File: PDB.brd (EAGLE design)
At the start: 130.3 x 166.9 mm, 49 parts, among them J1 B06B-HCMKK, J2 B06B-HCMKK, J3 SS-6488-NF-A431, J4 SS-6488-NF-A431, J5 B06B-HCMKK, J6 B03B-HCMKS, J7 B03B-HCMKS, J8 SS-6488-NF-A431

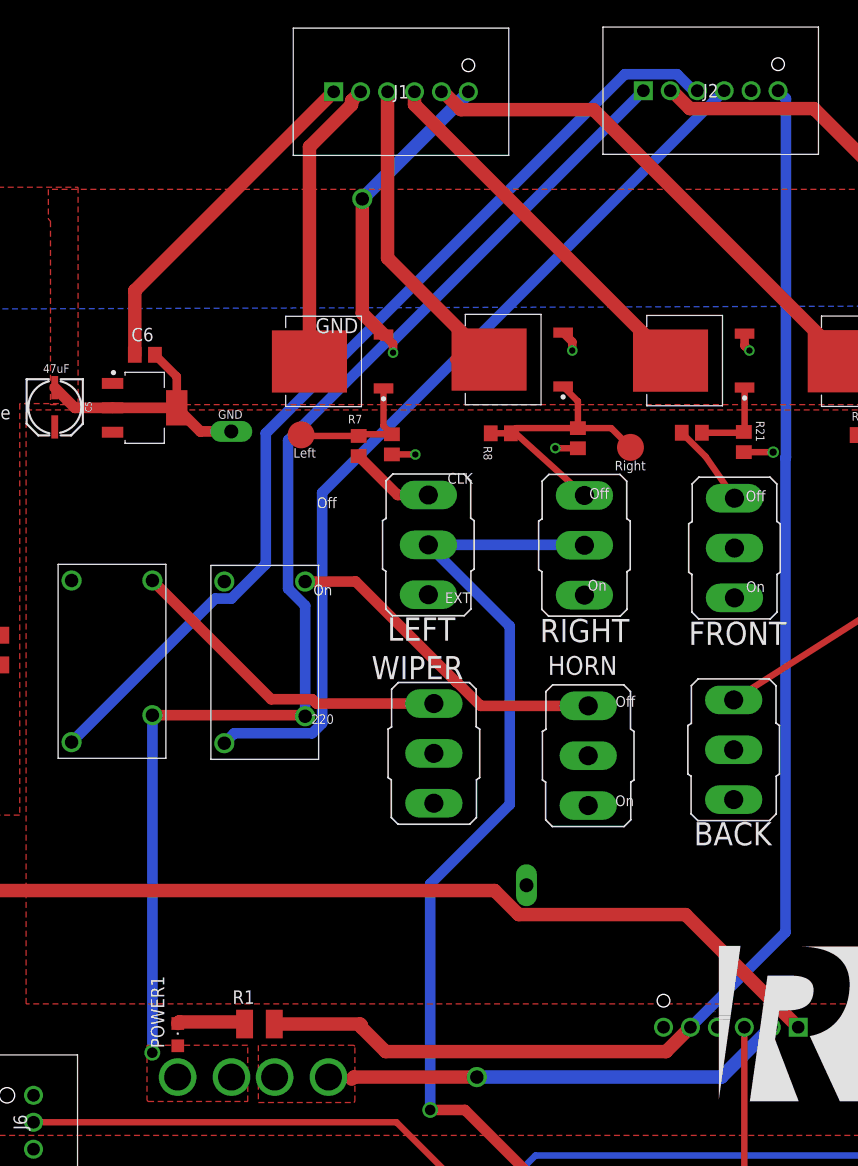
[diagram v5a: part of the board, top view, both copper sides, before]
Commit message: Widen the traces of independent 12V and indipendent ground
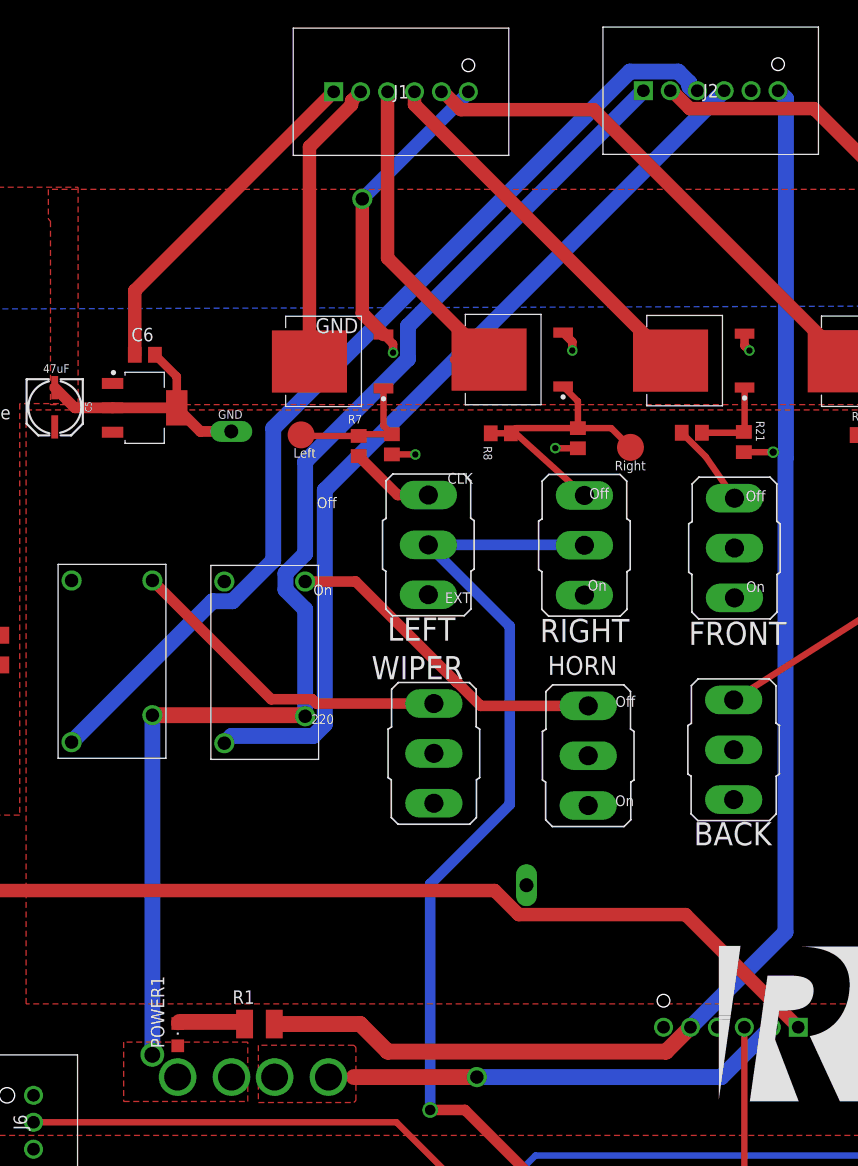
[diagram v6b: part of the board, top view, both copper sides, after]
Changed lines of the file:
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@@
 <vertex x="41.2" y="47.3"/>
 <vertex x="50.2" y="47.3"/>
-<vertex x="50.3" y="47.4"/>
-<vertex x="50.3" y="52.6"/>
+<vertex x="50.4" y="47.5"/>
+<vertex x="50.4" y="52.5"/>
 <vertex x="50.2" y="52.7"/>
 </polygon>
-<wire x1="89.56" y1="54.4" x2="84.86" y2="49.7" width="1.27" layer="16"/>
-<wire x1="84.86" y1="49.7" x2="61.8" y2="49.7" width="1.27" layer="16"/>
+<wire x1="89.56" y1="54.4" x2="84.86" y2="49.7" width="1.5" layer="16"/>
+<wire x1="84.86" y1="49.7" x2="61.8" y2="49.7" width="1.5" layer="16"/>
 <via x="61.8" y="49.7" extent="1-16" drill="1.27"/>
-<wire x1="61.8" y1="49.7" x2="50.2" y2="49.7" width="1.27" layer="1"/>
-<wire x1="50.2" y1="49.7" x2="50" y2="49.5" width="1.27" layer="1"/>
+<wire x1="61.8" y1="49.7" x2="50.2" y2="49.7" width="1.5" layer="1"/>
+<wire x1="47.812" y1="49.7" x2="50.2" y2="49.7" width="0" layer="19" extent="1-1"/>
+<wire x1="42.732" y1="49.7" x2="47.812" y2="49.7" width="0" layer="19" extent="1-1"/>
 </signal>
 <signal name="IGND">
@@
 <contactref element="R1" pad="2"/>
 <contactref element="J2" pad="6"/>
-<wire x1="81.94" y1="54.4" x2="79.64" y2="52.1" width="1.27" layer="1"/>
-<wire x1="79.64" y1="52.1" x2="53.2" y2="52.1" width="1.27" layer="1"/>
-<wire x1="53.2" y1="52.1" x2="50.9" y2="54.4" width="1.27" layer="1"/>
-<wire x1="50.9" y1="54.4" x2="50.9" y2="54.6" width="1.27" layer="1"/>
-<wire x1="50.9" y1="54.6" x2="50.8" y2="54.7" width="1.27" layer="1"/>
-<wire x1="50.8" y1="54.7" x2="42.7" y2="54.7" width="1.27" layer="1"/>
-<wire x1="81.94" y1="54.4" x2="90.9" y2="63.36" width="1" layer="16"/>
+<wire x1="81.94" y1="54.4" x2="79.64" y2="52.1" width="1.5" layer="1"/>
+<wire x1="79.64" y1="52.1" x2="53.4" y2="52.1" width="1.5" layer="1"/>
+<wire x1="53.4" y1="52.1" x2="50.8" y2="54.7" width="1.5" layer="1"/>
+<wire x1="50.8" y1="54.7" x2="42.7" y2="54.7" width="1.5" layer="1"/>
+<wire x1="81.94" y1="54.4" x2="90.9" y2="63.36" width="1.5" layer="16"/>
 <wire x1="90.9" y1="108.08209375" x2="90.9406" y2="108.12269375" width="1" layer="16"/>
-<wire x1="90.9406" y1="108.12269375" x2="90.9406" y2="141.9594" width="1" layer="16"/>
-<wire x1="90.9406" y1="141.9594" x2="90.2" y2="142.7" width="1" layer="16"/>
-<wire x1="90.9" y1="63.36" x2="90.9" y2="108.08209375" width="1" layer="16"/>
+<wire x1="90.9406" y1="108.12269375" x2="90.9406" y2="141.9594" width="1.5" layer="16"/>
+<wire x1="90.9406" y1="141.9594" x2="90.2" y2="142.7" width="1.5" layer="16"/>
+<wire x1="90.9" y1="63.36" x2="90.9" y2="108.08209375" width="1.5" layer="16"/>
 </signal>
 <signal name="ISOENABLE">
@@
 <contactref element="U$5" pad="SWA"/>
 <polygon width="0.0762" layer="1">
-<vertex x="30.7" y="52.5"/>
-<vertex x="30.7" y="47.5"/>
-<vertex x="30.8" y="47.4"/>
+<vertex x="28.5" y="53"/>
+<vertex x="28.5" y="47.4"/>
 <vertex x="40.2" y="47.4"/>
-<vertex x="40.2" y="52.7"/>
-<vertex x="30.7" y="52.7"/>
+<vertex x="40.2" y="53"/>
 </polygon>
-<wire x1="31.21" y1="83.82" x2="31.21" y2="52.01" width="1" layer="16"/>
-<wire x1="31.21" y1="52.01" x2="31.2" y2="52" width="1" layer="16"/>
-<via x="31.2" y="52" extent="1-16" drill="1"/>
-<wire x1="45.51" y1="83.82" x2="45.61" y2="83.72" width="1" layer="16"/>
-<wire x1="31.21" y1="83.82" x2="45.51" y2="83.82" width="1" layer="1"/>
-<wire x1="45.51" y1="83.82" x2="45.61" y2="83.72" width="1" layer="1"/>
-<wire x1="53.42133125" y1="119.1556" x2="53.9556" y2="119.1556" width="1" layer="16"/>
-<wire x1="53.9556" y1="119.1556" x2="77.5" y2="142.7" width="1" layer="16"/>
-<wire x1="45.61" y1="83.72" x2="45.61" y2="94.150325" width="1" layer="16"/>
-<wire x1="45.61" y1="94.150325" x2="44.0051" y2="95.755225" width="1" layer="16"/>
-<wire x1="44.0051" y1="95.755225" x2="44.0051" y2="109.73936875" width="1" layer="16"/>
-<wire x1="44.0051" y1="109.73936875" x2="53.42133125" y2="119.1556" width="1" layer="16"/>
+<wire x1="43.7551" y1="95.651675" x2="43.7551" y2="97.188325" width="1.5" layer="16"/>
+<wire x1="45.61" y1="83.72" x2="45.61" y2="93.796775" width="1.5" layer="16"/>
+<wire x1="55.3056" y1="120.5056" x2="77.5" y2="142.7" width="1.5" layer="16"/>
+<wire x1="45.61" y1="93.796775" x2="43.7551" y2="95.651675" width="1.5" layer="16"/>
+<wire x1="43.7551" y1="97.188325" x2="45.61" y2="99.043225" width="1.5" layer="16"/>
+<wire x1="55.3056" y1="117.41778125" x2="55.3056" y2="120.5056" width="1.5" layer="16"/>
+<wire x1="45.61" y1="99.043225" x2="45.61" y2="107.72218125" width="1.5" layer="16"/>
+<wire x1="45.61" y1="107.72218125" x2="55.3056" y2="117.41778125" width="1.5" layer="16"/>
+<wire x1="31.2" y1="83.81" x2="31.21" y2="83.82" width="1.5" layer="16"/>
+<wire x1="31.21" y1="83.82" x2="45.51" y2="83.82" width="1.5" layer="1"/>
+<wire x1="45.51" y1="83.82" x2="45.61" y2="83.72" width="1.5" layer="1"/>
+<wire x1="31.21" y1="83.82" x2="31.21" y2="51.81" width="1.5" layer="16"/>
+<wire x1="31.21" y1="51.81" x2="31.2" y2="51.8" width="1.5" layer="16"/>
+<via x="31.2" y="51.8" extent="1-16" drill="1.5"/>
 </signal>
 <signal name="N$10">
@@
 <contactref element="POWER1" pad="C"/>
 <wire x1="39.9" y1="54.7" x2="39.7" y2="54.9" width="1.27" layer="1"/>
-<wire x1="39.7" y1="54.9" x2="33.75" y2="54.9" width="1.27" layer="1"/>
+<wire x1="39.7" y1="54.9" x2="33.75" y2="54.9" width="1.5" layer="1"/>
 <wire x1="33.6" y1="54.75" x2="33.75" y2="54.9" width="1.27" layer="1"/>
 </signal>
@@
 <contactref element="U$6" pad="SWB"/>
 <contactref element="J2" pad="3"/>
-<wire x1="23.59" y1="81.28" x2="37.1251" y2="94.8151" width="1" layer="16"/>
-<wire x1="37.1251" y1="94.8151" x2="38.654775" y2="94.8151" width="1" layer="16"/>
-<wire x1="38.654775" y1="94.8151" x2="41.9" y2="98.060325" width="1" layer="16"/>
-<wire x1="41.9" y1="98.060325" x2="41.9" y2="110.4" width="1" layer="16"/>
 <wire x1="82.23543125" y1="142.7" x2="82.58" y2="142.7" width="1" layer="16"/>
-<wire x1="80.68303125" y1="144.2524" x2="82.23543125" y2="142.7" width="1" layer="16"/>
-<wire x1="41.9" y1="110.4" x2="75.7524" y2="144.2524" width="1" layer="16"/>
-<wire x1="75.7524" y1="144.2524" x2="80.68303125" y2="144.2524" width="1" layer="16"/>
+<wire x1="80.78658125" y1="144.5024" x2="81.8424" y2="143.44658125" width="1.5" layer="16"/>
+<wire x1="23.59" y1="81.28" x2="36.8751" y2="94.5651" width="1.5" layer="16"/>
+<wire x1="36.8751" y1="94.5651" x2="38.758325" y2="94.5651" width="1.5" layer="16"/>
+<wire x1="76.2262125" y1="144.5024" x2="80.78658125" y2="144.5024" width="1.5" layer="16"/>
+<wire x1="38.758325" y1="94.5651" x2="42.6027" y2="98.409475" width="1.5" layer="16"/>
+<wire x1="42.6027" y1="98.409475" x2="42.6027" y2="110.8788875" width="1.5" layer="16"/>
+<wire x1="42.6027" y1="110.8788875" x2="76.2262125" y2="144.5024" width="1.5" layer="16"/>
+<wire x1="81.8424" y1="143.44658125" x2="81.8424" y2="143.09303125" width="1.5" layer="16"/>
+<wire x1="81.8424" y1="143.09303125" x2="82.23543125" y2="142.7" width="1.5" layer="16"/>
 </signal>
 <signal name="HORN">
 <contactref element="U$5" pad="SWB"/>
 <contactref element="J2" pad="4"/>
-<wire x1="46.274775" y1="82.1151" x2="47.2149" y2="83.055225" width="1" layer="16"/>
-<wire x1="47.2149" y1="104.7949" x2="85.12" y2="142.7" width="1" layer="16"/>
-<wire x1="47.2149" y1="83.055225" x2="47.2149" y2="104.7949" width="1" layer="16"/>
-<wire x1="37.99" y1="81.18" x2="38.9251" y2="82.1151" width="1" layer="16"/>
-<wire x1="38.9251" y1="82.1151" x2="46.274775" y2="82.1151" width="1" layer="16"/>
+<wire x1="46.378325" y1="81.8651" x2="47.4649" y2="82.951675" width="1.5" layer="16"/>
+<wire x1="84.3824" y1="141.95341875" x2="84.3824" y2="141.9624" width="1.5" layer="16"/>
+<wire x1="84.3824" y1="141.9624" x2="85.12" y2="142.7" width="1.5" layer="16"/>
+<wire x1="47.4649" y1="82.951675" x2="47.4649" y2="105.03591875" width="1.5" layer="16"/>
+<wire x1="47.4649" y1="105.03591875" x2="84.3824" y2="141.95341875" width="1.5" layer="16"/>
+<wire x1="37.99" y1="81.18" x2="38.6751" y2="81.8651" width="1.5" layer="16"/>
+<wire x1="38.6751" y1="81.8651" x2="46.378325" y2="81.8651" width="1.5" layer="16"/>
 </signal>
 <signal name="MOSI_SW">
